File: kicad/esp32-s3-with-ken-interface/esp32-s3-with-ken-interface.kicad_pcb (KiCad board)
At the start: 4 copper layers, 50.8 x 81.3 mm, 38 parts, among them J1 TYPE-C-31-M-12, Q1 UMH3N, SW1 TSC015A03526A, U1 CH340C, U2 AMS1117-3.3, U3 XDZ254-2-15-W-2.5-G1, U4 ESP32-S3-WROOM-1, U5 PM254-2-15-W-8.5

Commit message: add KiCad project for xiaozhi AI with KEN interface
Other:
- board text added: "A"
- board text added: "B"
- board text added: "C"
- board text added: "D"
- board text added: "E"
- board text added: "F"
- board text removed: "A/PWM1"
- board text removed: "B/PWM2"
- board text removed: "C/PWM3"
- board text removed: "D/PWM4"
- board text removed: "PWM5"
- board text removed: "PWM6"

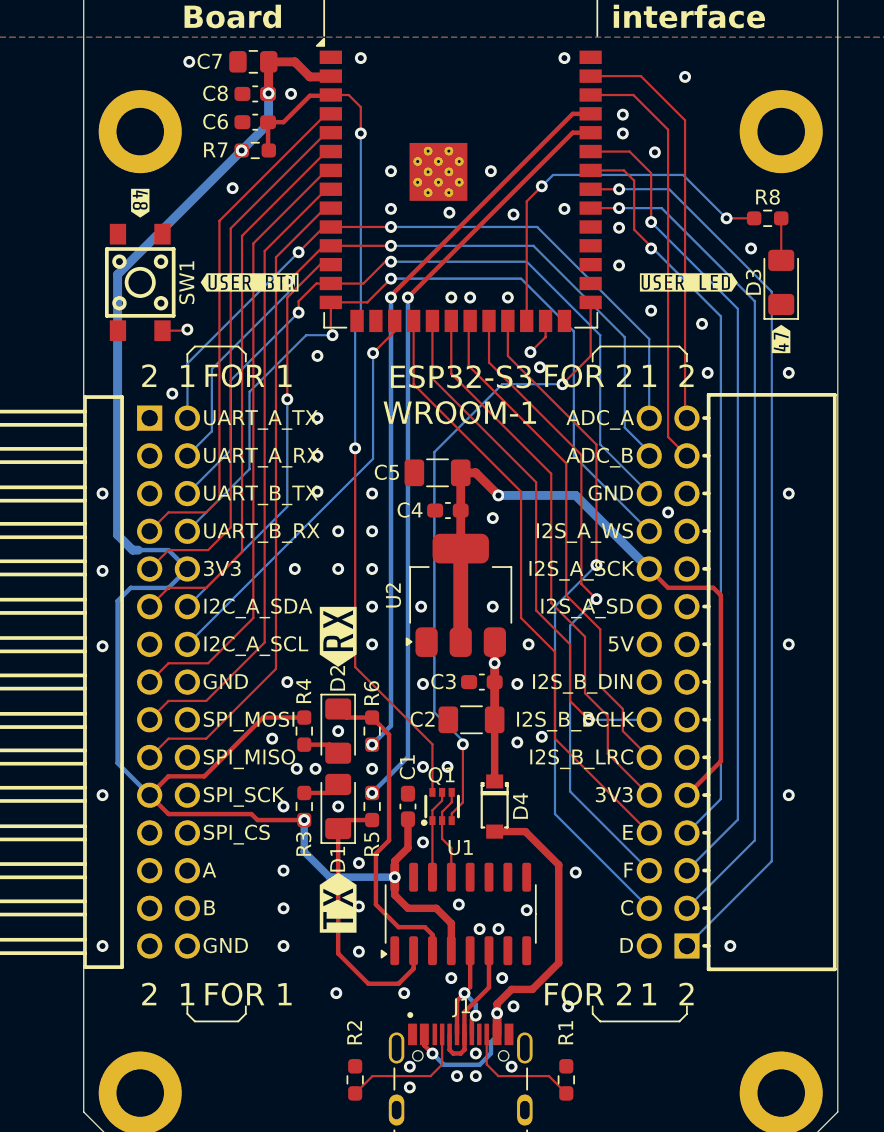
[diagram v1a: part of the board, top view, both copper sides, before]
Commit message: improve routing for ESP32-S3 board
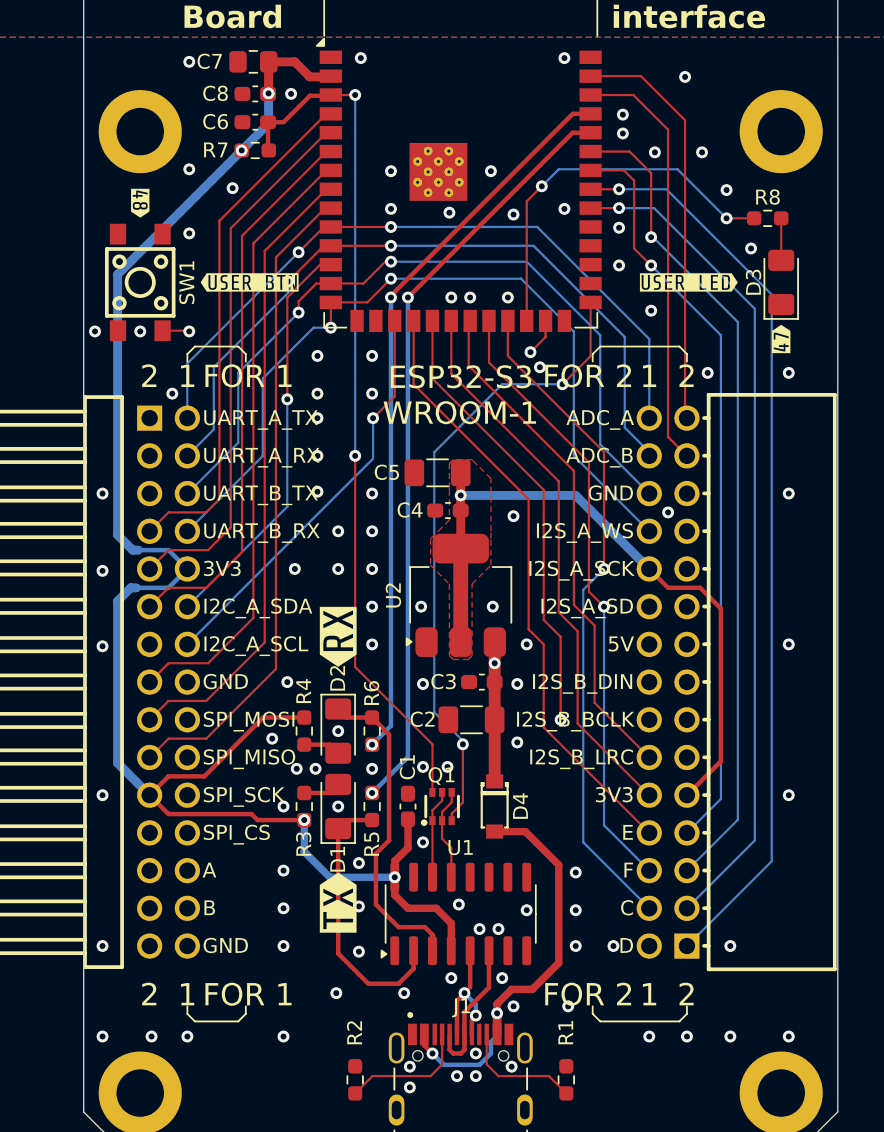
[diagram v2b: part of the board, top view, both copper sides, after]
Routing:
- net /IO11: track 66.4 -> 61.6 mm
- net /BTN_A: track 75.0 -> 73.6 mm
- net /BTN_B: track 78.2 -> 77.0 mm
- net +3V3: track 183.4 -> 182.3 mm
- net GND: vias 91 -> 109
- added copper zone on F.Cu, net +3V3

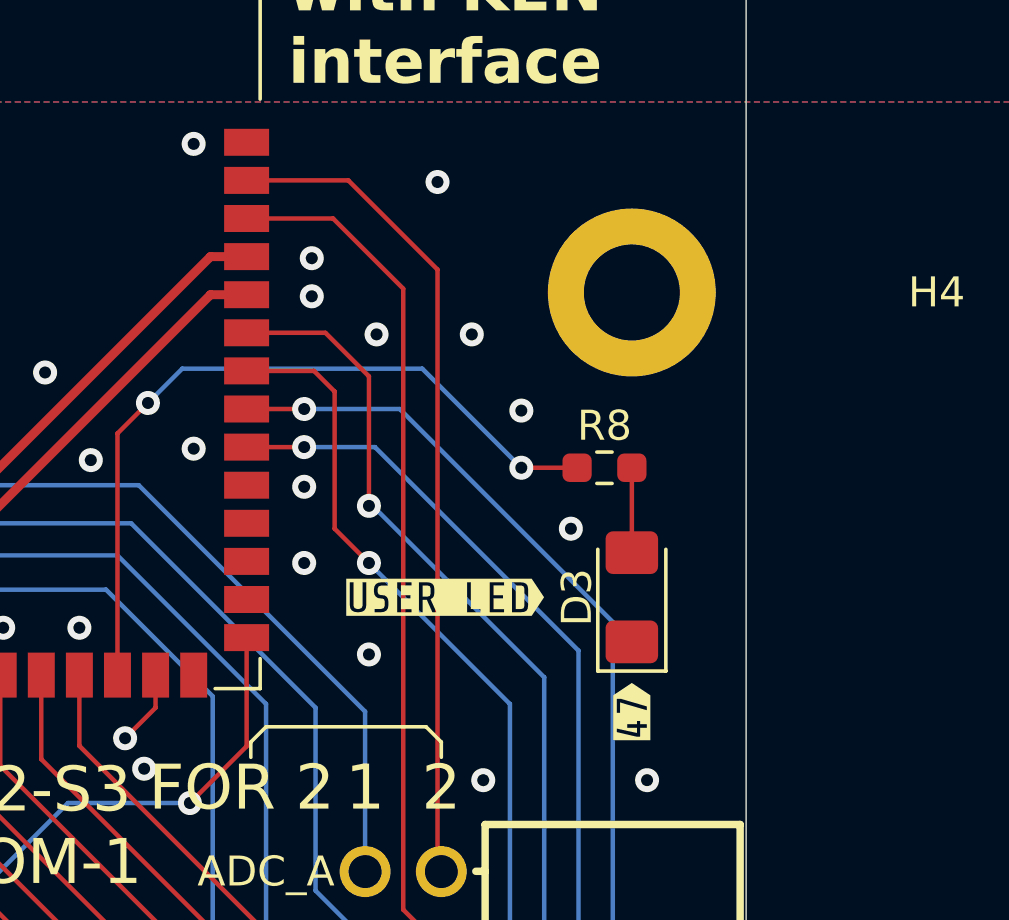
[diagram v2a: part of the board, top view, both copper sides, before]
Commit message: add boot button to ESP32-S3 board, add speaker to xiaozhi, improve xiaozhi board schematic and routing.
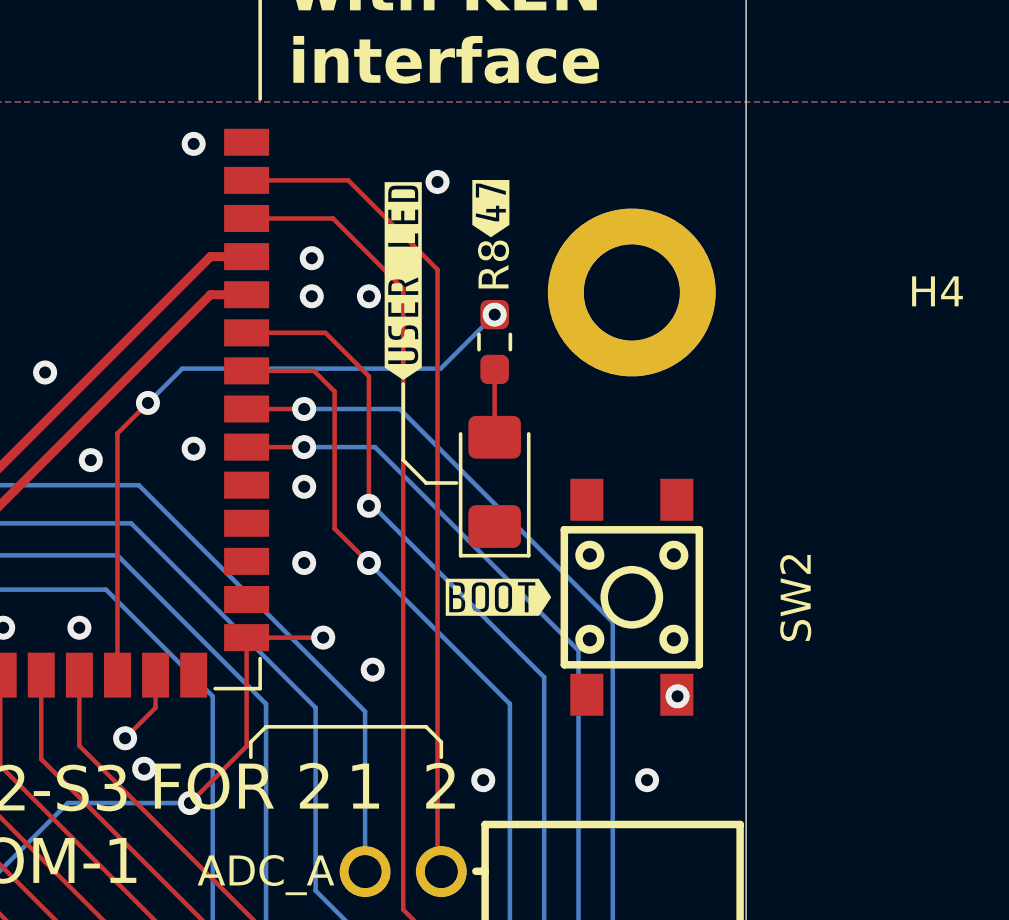
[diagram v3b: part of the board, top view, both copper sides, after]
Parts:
- removed kibuzzard-697171B1: G***, kibuzzard-697171B1
- removed kibuzzard-69717543: G***, kibuzzard-69717543
- added SW2: TSC015A03526A, TSC015A03526A:SW-SMD_4P-L4.5-W4.5-P3.00-LS6.8, F.Cu at (105.4, 62.2)
- added kibuzzard-69756FE8: G***, kibuzzard-69756FE8, F.Cu at (101.0, 62.2)
- added kibuzzard-6975703A: G***, kibuzzard-6975703A, F.Cu at (100.7, 49.3)
- added kibuzzard-6975704C: G***, kibuzzard-6975704C, F.Cu at (97.8, 51.7)
- moved D3 5.97 mm to (100.8, 58.4)
- moved R8 5.56 mm to (100.8, 53.7), turned to -90 degrees
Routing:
- net /IO0: track 42.8 -> 57.9 mm, vias 2 -> 4
- net /IO47: track 25.6 -> 22.3 mm
- net Net-(D3-A): track 2.83 -> 2.14 mm
- net GND: vias 109 -> 106

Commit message: final adjust, send to pcb maker
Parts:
- moved kibuzzard-69717533 1.40 mm to (68.2, 62.2)
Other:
- outline, holes or cut-outs redrawn
- board text added: "MCU Board"
- board text added: "version:1.0 date: 20260125"
- board text removed: "Controller Board"
- board text removed: "version:1.0 date: 20260123"

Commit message: fix labels, update manufacture files
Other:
- board text added: "with KEN Interface"
- board text removed: "with KEN interface"

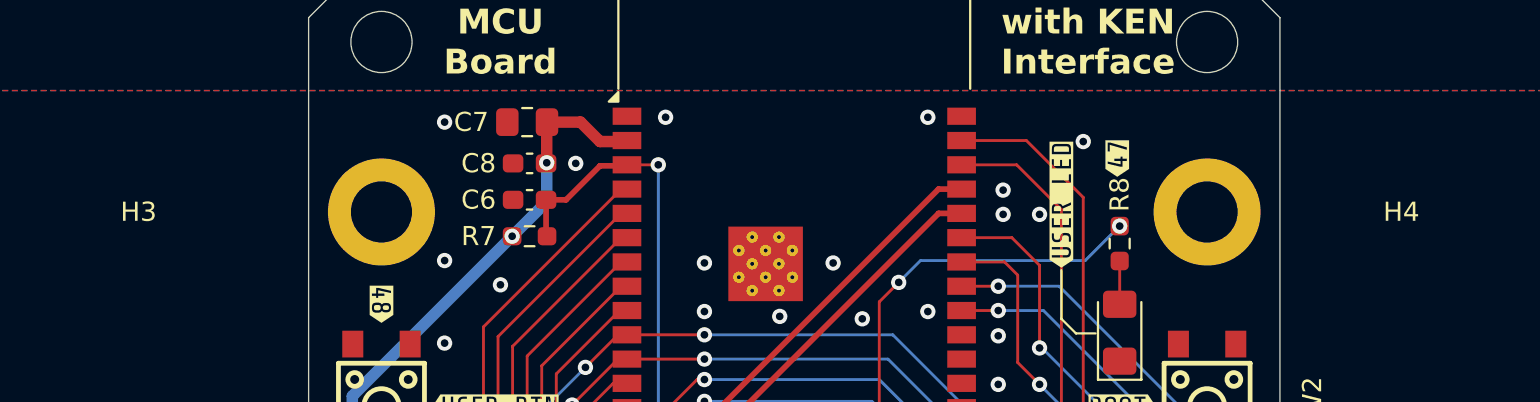
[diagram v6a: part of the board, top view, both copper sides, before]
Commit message: add reset button
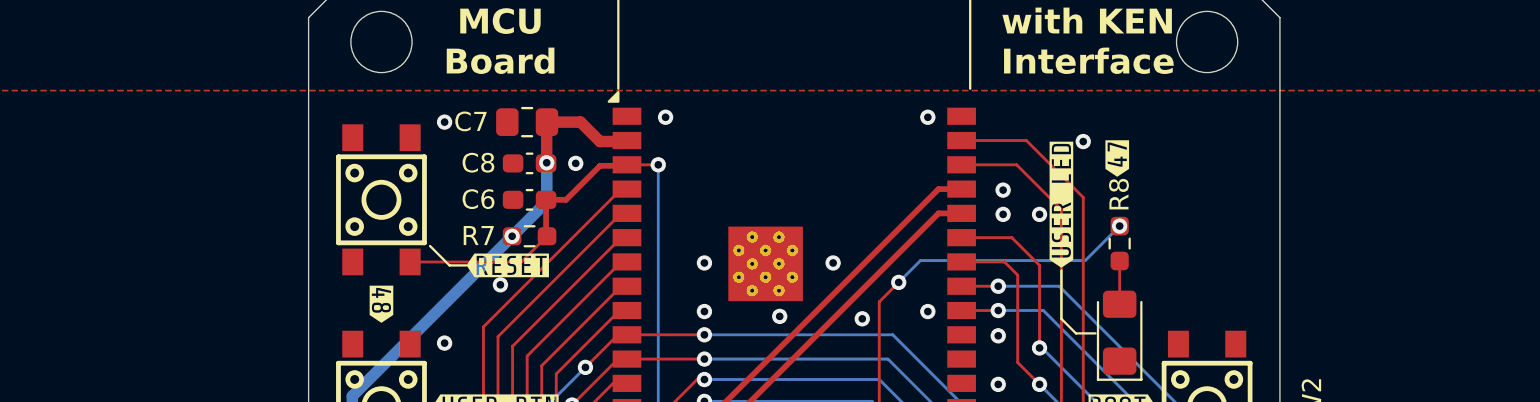
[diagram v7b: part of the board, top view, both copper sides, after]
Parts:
- removed H3, H4: MountHole, MountingHole:MountingHole_3.2mm_M3_DIN965_Pad
- added SW3: TSC015A03526A, TSC015A03526A:SW-SMD_4P-L4.5-W4.5-P3.00-LS6.8, F.Cu at (62.2, 51.4)
- added kibuzzard-69BBE7EF: G***, kibuzzard-69BBE7EF, F.Cu at (68.8, 54.9)
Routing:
- net /EN: track 57.7 -> 65.4 mm
- net GND: vias 106 -> 105
